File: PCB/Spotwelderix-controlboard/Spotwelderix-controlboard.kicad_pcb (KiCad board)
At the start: 2 copper layers, 103.4 x 56.4 mm, 27 parts, among them J1 Extender, J3 Switch_OnOFF, J4 FAN, P1 Display, P2 CONN_01X08, Q1 DMG1012T-7, Q2 DMG1012T-7, U1 NodeMCU32, U2 ADS1115_Module, U3 LM7805M_TO263

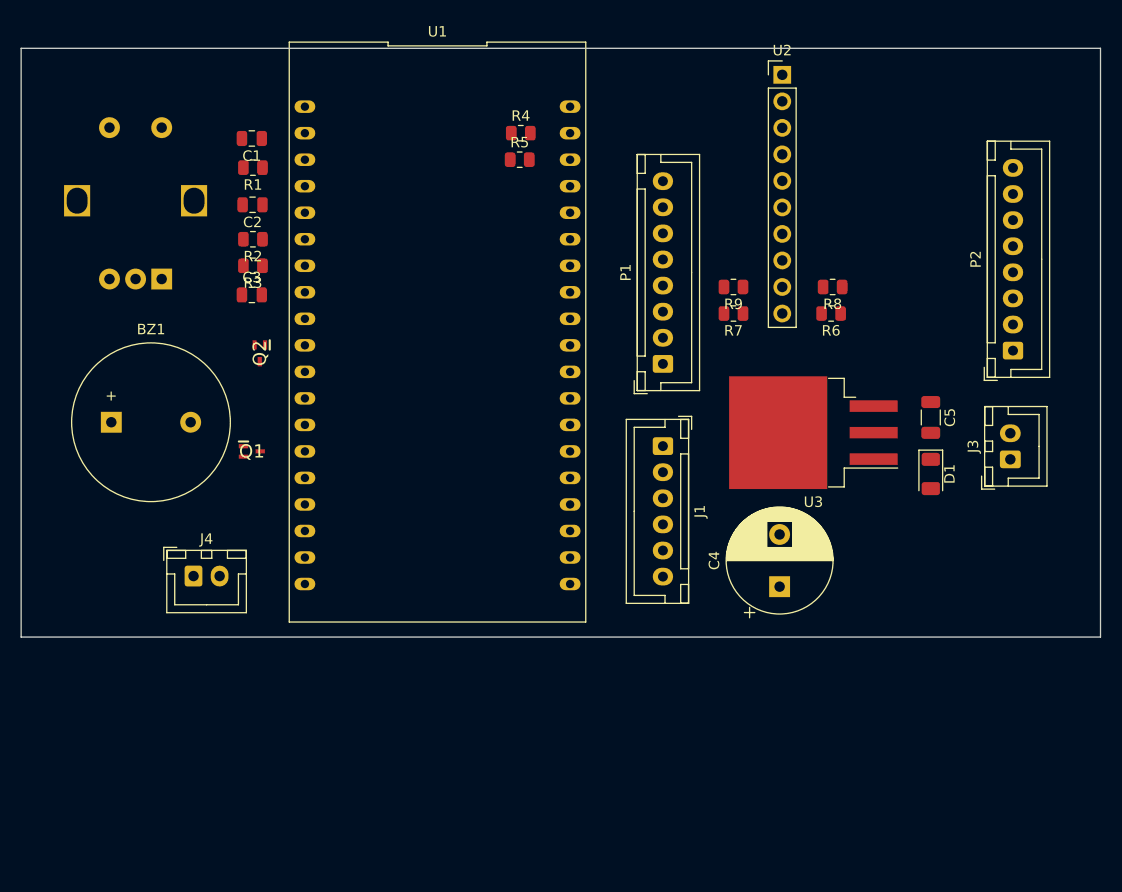
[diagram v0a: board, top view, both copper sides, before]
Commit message: power pcb added
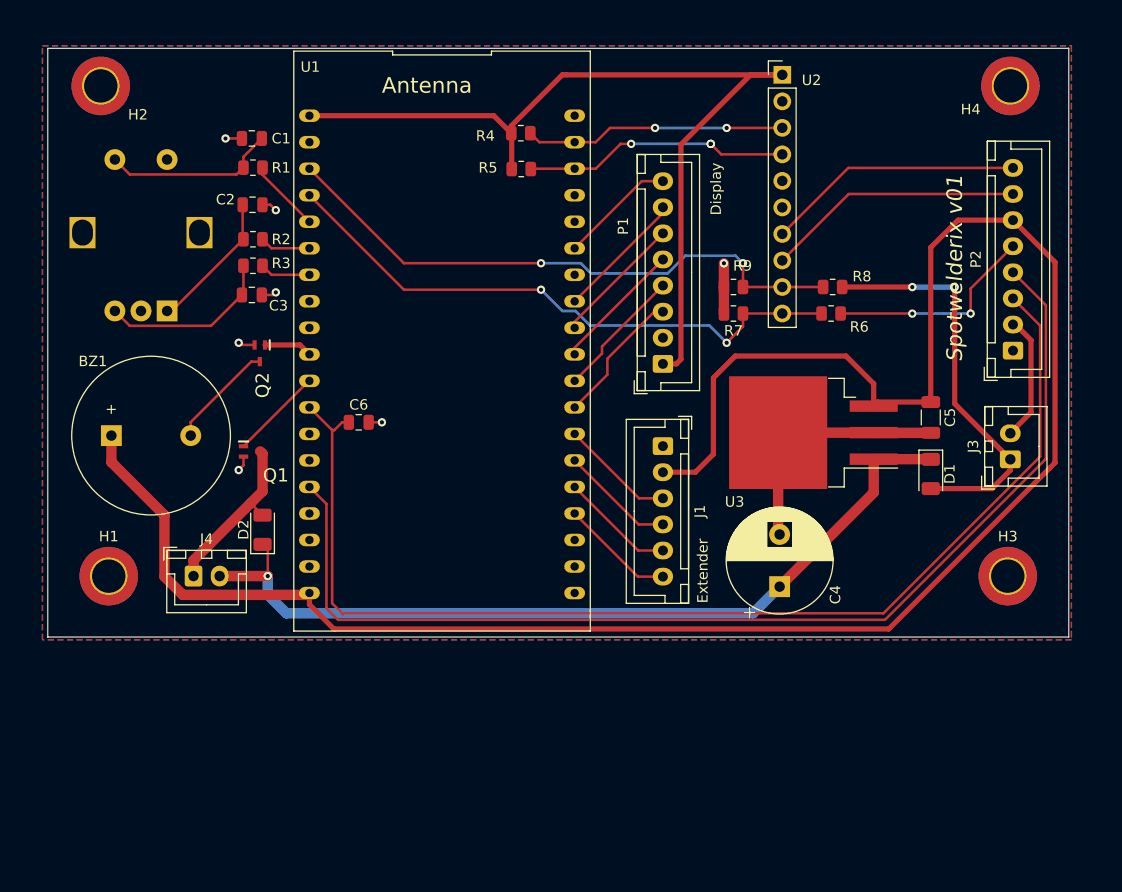
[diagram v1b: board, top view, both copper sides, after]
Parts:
- added C6: 10n, Capacitor_SMD:C_0805_2012Metric, F.Cu at (44.8, 48.3)
- added D2: D, Diode_SMD:D_1206_3216Metric, F.Cu at (35.6, 58.5)
- added H1: MountingHole, MountingHole:MountingHole_3.2mm_M3_DIN965_Pad_TopBottom, F.Cu at (20.8, 63.0)
- added H2: MountingHole, MountingHole:MountingHole_3.2mm_M3_DIN965_Pad_TopBottom, F.Cu at (20.1, 16.0)
- added H3: MountingHole, MountingHole:MountingHole_3.2mm_M3_DIN965_Pad_TopBottom, F.Cu at (106.9, 63.0)
- added H4: MountingHole, MountingHole:MountingHole_3.2mm_M3_DIN965_Pad_TopBottom, F.Cu at (107.2, 16.0)
- moved ENC1 3.10 mm to (26.4, 37.6)
- moved BZ1 1.28 mm to (21.1, 49.5)
- moved U1 0.97 mm to (52.8, 41.8)
- moved R5 0.91 mm to (60.3, 24.0)
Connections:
- J4 pad 2: +5V -> Net-(C4-Pad1)
- R4 pad 2: SDA -> SCL
- R5 pad 2: SCL -> SDA
- R6 pad 2: Net-(R6-Pad2) -> A3_VCC_ADC
- R7 pad 1: Net-(R6-Pad2) -> A3_VCC_ADC
- R8 pad 2: Net-(R8-Pad2) -> A2_ProbeADC
- R9 pad 1: Net-(R8-Pad2) -> A2_ProbeADC
- U1 pad 12: Dallas -> Gate_logic
- U1 pad 15: Gate_logic -> Dallas
- U1 pad 3: Net-(U1-Pad3) -> A2_ProbeADC
- U1 pad 36: SCL -> SDA
- U1 pad 37: SDA -> SCL
- U1 pad 4: Net-(U1-Pad4) -> A3_VCC_ADC
- U2 pad 10: Net-(R6-Pad2) -> A3_VCC_ADC
- U2 pad 9: Net-(R8-Pad2) -> A2_ProbeADC
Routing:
- net +5V: track 0.00 -> 197.0 mm
- net Gate_logic: track 0.00 -> 112.3 mm
- net Dallas: track 0.00 -> 107.2 mm
- net +3V3: track 0.00 -> 87.5 mm
- net Net-(C4-Pad1): track 0.00 -> 81.9 mm, vias 0 -> 1
- net A3_VCC_ADC: track 0.00 -> 56.8 mm, vias 0 -> 2
- net A2_ProbeADC: track 0.00 -> 56.6 mm, vias 0 -> 2
- net VCC: track 0.00 -> 38.9 mm, vias 0 -> 2
- net GND: track 0.00 -> 38.1 mm, vias 0 -> 7
- net SDA: track 0.00 -> 25.5 mm, vias 0 -> 3
- net SCL: track 0.00 -> 25.1 mm, vias 0 -> 2
- net R_Schunt_H: track 0.00 -> 24.7 mm
- net R_Schunt_L: track 0.00 -> 24.7 mm
- net Probe: track 0.00 -> 20.6 mm, vias 0 -> 2
- net Net-(C3-Pad1): track 0.00 -> 16.8 mm
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- added copper zone on F.Cu, net +5V
- added copper zone on B.Cu, net GND
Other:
- board size 103.4 x 56.4 mm -> 97.8 x 56.4 mm
- net class Default: clearance 0.3 -> 0.2
- net class Power: clearance 0.5 -> 0.3
- rule trace_clearance: 0.3 -> 0.2
- board text added: "Antenna"
- board text added: "Display"
- board text added: "Extender"
- board text added: "Spotwelderix v01"

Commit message: power pcb updated, added safe power for driver
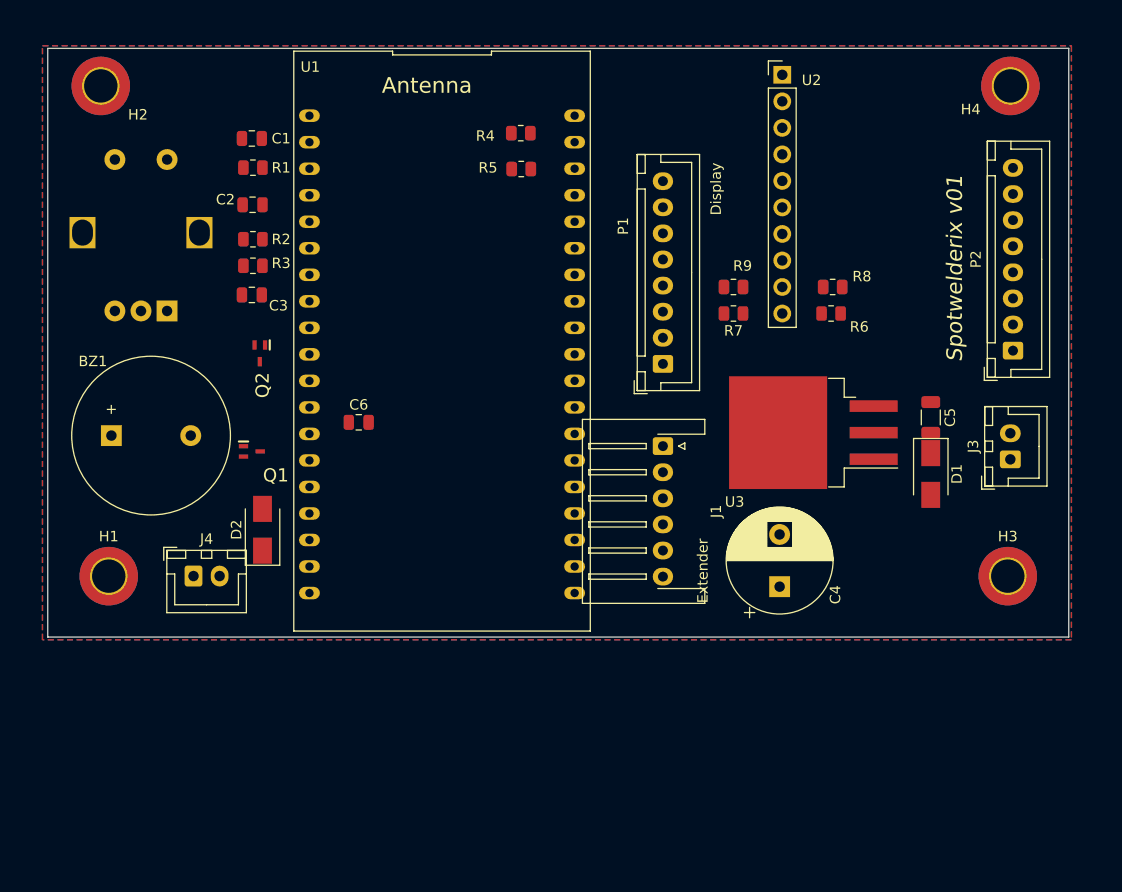
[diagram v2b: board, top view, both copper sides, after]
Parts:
- D1, D2: footprint Diode_SMD:D_1206_3216Metric -> Diode_SMD:D_SMA
- J1: footprint Connector_JST:JST_XH_B6B-XH-A_1x06_P2.50mm_Vertical -> Connector_JST:JST_XH_S6B-XH-A-1_1x06_P2.50mm_Horizontal
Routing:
- net +5V: track 197.0 -> 0.00 mm
- net Gate_logic: track 112.3 -> 0.00 mm
- net Dallas: track 107.2 -> 0.00 mm
- net +3V3: track 87.5 -> 0.00 mm
- net Net-(C4-Pad1): track 81.9 -> 0.00 mm, vias 1 -> 0
- net A3_VCC_ADC: track 56.8 -> 0.00 mm, vias 2 -> 0
- net A2_ProbeADC: track 56.6 -> 0.00 mm, vias 2 -> 0
- net VCC: track 38.9 -> 0.00 mm, vias 2 -> 0
- net GND: track 38.1 -> 0.00 mm, vias 7 -> 0
- net SDA: track 25.5 -> 0.00 mm, vias 3 -> 0
- net SCL: track 25.1 -> 0.00 mm, vias 2 -> 0
- net R_Schunt_H: track 24.7 -> 0.00 mm
- net R_Schunt_L: track 24.7 -> 0.00 mm
- net Probe: track 20.6 -> 0.00 mm, vias 2 -> 0
- net Net-(C3-Pad1): track 16.8 -> 0.00 mm
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
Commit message: ena powerpcb added
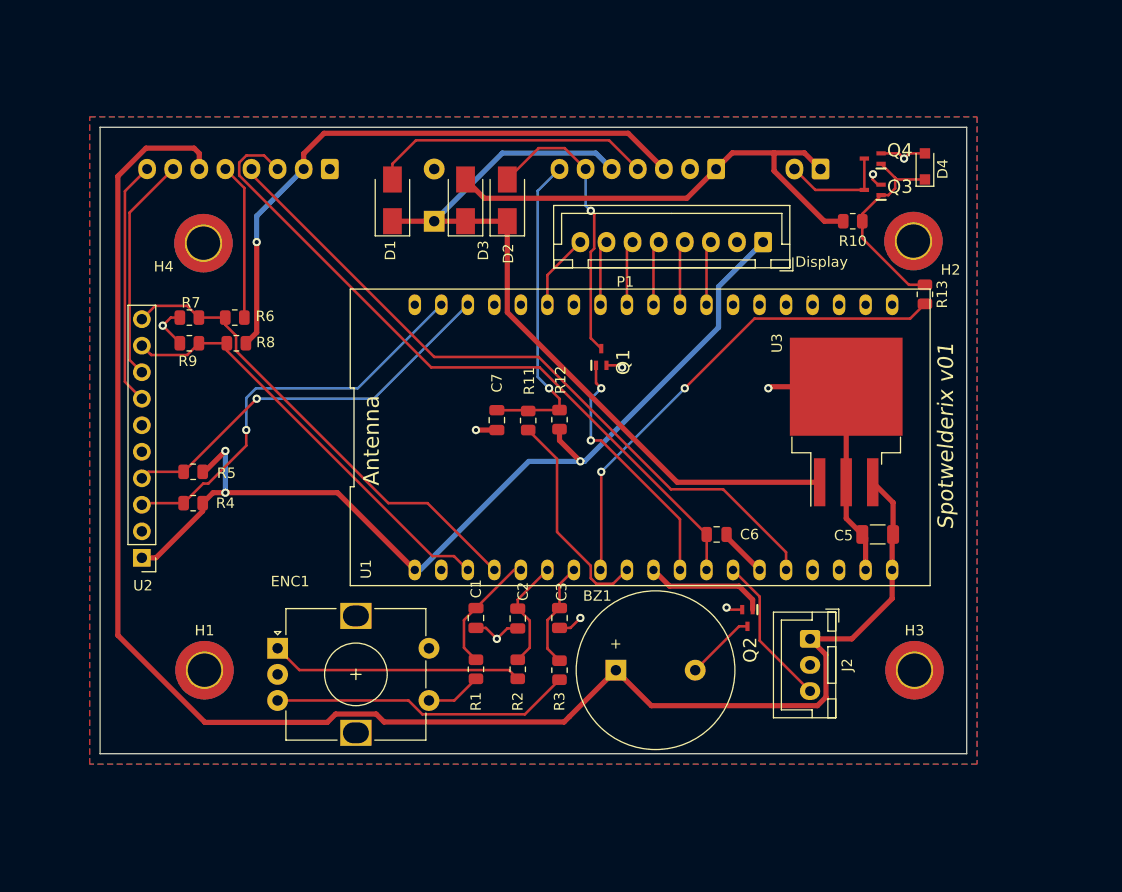
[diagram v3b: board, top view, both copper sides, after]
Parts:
- removed J1: Extender, Connector_JST:JST_XH_S6B-XH-A-1_1x06_P2.50mm_Horizontal
- added C7: 100n, Capacitor_SMD:C_0805_2012Metric, F.Cu at (58.0, 48.0)
- added D3: D, Diode_SMD:D_SMA, F.Cu at (55.0, 27.0)
- added D4: 3.6V, Diode_SMD:D_SOD-323_HandSoldering, F.Cu at (99.0, 23.8)
- added J2: LEDs, Connector_JST:JST_XH_B3B-XH-A_1x03_P2.50mm_Vertical, F.Cu at (88.0, 69.0)
- added Q3: DMG1012T-7, SamacSys_Parts:SOT50P160X80-3N, F.Cu at (94.0, 26.0)
- added Q4: DMG1012T-7, SamacSys_Parts:SOT50P160X80-3N, F.Cu at (94.0, 23.0)
- added R10: 10k, Resistor_SMD:R_0805_2012Metric, F.Cu at (92.1, 29.0)
- added R11: 100, Resistor_SMD:R_0805_2012Metric, F.Cu at (61.0, 48.1)
- added R12: 10k, Resistor_SMD:R_0805_2012Metric, F.Cu at (64.0, 48.0)
- added R13: 100, Resistor_SMD:R_0805_2012Metric, F.Cu at (99.0, 36.0)
- C1, C2, C3: value 100n -> 100p
- C4, P2: moved to B.Cu
- ENC1: moved to F.Cu
- J3: footprint Connector_JST:JST_XH_B2B-XH-A_1x02_P2.50mm_Vertical -> Connector_JST:JST_XH_B7B-XH-A_1x07_P2.50mm_Vertical; moved to B.Cu
- J4: value FAN -> Int_Charger_supply; moved to B.Cu
- moved H2 79.2 mm to (97.9, 30.9)
- moved H4 78.7 mm to (29.9, 31.1)
- moved U2 76.8 mm to (24.0, 61.2), turned to 180 degrees
- moved J4 71.6 mm to (89.0, 24.0), turned to 180 degrees
- moved P2 67.7 mm to (42.0, 24.0), turned to 180 degrees
- moved D1 57.8 mm to (48.0, 27.0), turned to 90 degrees
- moved R8 57.4 mm to (33.1, 40.7)
- moved R6 57.1 mm to (32.9, 38.2)
- moved BZ1 53.3 mm to (69.4, 72.0)
- moved Q2 53.1 mm to (82.0, 67.0)
- moved R1 52.6 mm to (56.0, 71.9), turned to 270 degrees
- moved R9 52.4 mm to (28.6, 40.7)
- moved R7 52.1 mm to (28.6, 38.2)
- moved C1 50.7 mm to (56.0, 67.0), turned to 270 degrees
- moved R3 48.6 mm to (64.0, 72.0), turned to 270 degrees
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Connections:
- C1 pad 1: Net-(C1-Pad1) -> UI_RotEnc_Push
- C2 pad 2: Net-(C2-Pad2) -> UI_RotEnc_A
- C3 pad 1: Net-(C3-Pad1) -> UI_RotEnc_B
- C4 pad 1: Net-(C4-Pad1) -> /LM7805_in
- D1 pad 1: Net-(C4-Pad1) -> /LM7805_in
- D1 pad 2: VCC -> Net-(D1-Pad2)
- D2 pad 1: Net-(C4-Pad1) -> /LM7805_in
- D2 pad 2: Net-(D2-Pad2) -> FAN_GND
- ENC1 pad A: Net-(C2-Pad2) -> Net-(ENC1-PadA)
- ENC1 pad B: Net-(C3-Pad1) -> Net-(ENC1-PadB)
- ENC1 pad S2: Net-(C1-Pad1) -> Net-(ENC1-PadS2)
- J3 pad 1: VCC -> ExtPower
- J3 pad 2: PowerVCC -> GND
- J4 pad 1: Net-(D2-Pad2) -> ExtPower
- J4 pad 2: Net-(C4-Pad1) -> Net-(J4-Pad2)
- P2 pad 2: PowerVCC -> VCC
- Q1 pad 3: Net-(D2-Pad2) -> FAN_GND
- R1 pad 2: Net-(C1-Pad1) -> Net-(ENC1-PadS2)
- R2 pad 2: Net-(C2-Pad2) -> Net-(ENC1-PadA)
- R3 pad 2: Net-(C3-Pad1) -> Net-(ENC1-PadB)
- U1 pad 13: Net-(U1-Pad13) -> LED
- U1 pad 8: Net-(U1-Pad8) -> ChargDisEna
- U1 pad 9: Net-(U1-Pad9) -> Ext_Trigger
- U3 pad 1: Net-(C4-Pad1) -> /LM7805_in
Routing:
- net +5V: track 0.00 -> 158.0 mm
- net +3V3: track 0.00 -> 91.8 mm, vias 0 -> 3
- net /LM7805_in: track 0.00 -> 76.7 mm
- net Dallas: track 0.00 -> 68.4 mm
- net Gate_logic: track 0.00 -> 68.1 mm
- net VCC: track 0.00 -> 57.2 mm, vias 0 -> 1
- net GND: track 0.00 -> 53.4 mm, vias 0 -> 9
- net ExtPower: track 0.00 -> 47.5 mm
- net ChargDisEna: track 0.00 -> 47.1 mm, vias 0 -> 2
- net A3_VCC_ADC: track 0.00 -> 46.0 mm
- net A2_ProbeADC: track 0.00 -> 41.5 mm
- net SCL: track 0.00 -> 39.3 mm, vias 0 -> 1
- net SDA: track 0.00 -> 38.1 mm, vias 0 -> 1
- net Net-(C7-Pad1): track 0.00 -> 30.9 mm, vias 0 -> 1
- net Net-(ENC1-PadB): track 0.00 -> 28.9 mm
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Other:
- board size 97.8 x 56.4 mm -> 83 x 60 mm
- board text removed: "Extender"

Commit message: ordered version v01
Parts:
- removed D1: D, Diode_SMD:D_SMA
- removed D4: 3.6V, Diode_SMD:D_SOD-323_HandSoldering
- removed J4: Int_Charger_supply, Connector_JST:JST_XH_B2B-XH-A_1x02_P2.50mm_Vertical
- removed Q3, Q4: DMG1012T-7, SamacSys_Parts:SOT50P160X80-3N
- removed R10: 10k, Resistor_SMD:R_0805_2012Metric
- removed R13: 100, Resistor_SMD:R_0805_2012Metric
- removed R4, R5: 3k3, Resistor_SMD:R_0805_2012Metric
- removed U2: ADS1115_Module, Connector_PinHeader_2.54mm:PinHeader_1x10_P2.54mm_Vertical
- added J1: ChargerPower, Connector_JST:JST_XH_S5B-XH-A_1x05_P2.50mm_Horizontal, F.Cu at (34.8, 68.3)
- added Q5: AO3400A, Package_TO_SOT_SMD:SOT-23, F.Cu at (55.1, 31.9)
- added R14: 100, Resistor_SMD:R_0805_2012Metric, F.Cu at (29.9, 66.5)
- C7: value 100n -> 100p
- J3: value Switch_OnOFF -> ExtPwr_FAn; footprint Connector_JST:JST_XH_B7B-XH-A_1x07_P2.50mm_Vertical -> Connector_JST:JST_XH_B4B-XH-A_1x04_P2.50mm_Vertical
- P1: footprint Connector_JST:JST_XH_B8B-XH-A_1x08_P2.50mm_Vertical -> Connector_JST:JST_XH_S8B-XH-A_1x08_P2.50mm_Horizontal
- P2: value CONN_01X08 -> PowerPCB; footprint Connector_JST:JST_XH_B8B-XH-A_1x08_P2.50mm_Vertical -> Connector_JST:JST_XH_B9B-XH-A_1x09_P2.50mm_Vertical
- Q1, Q2: value DMG1012T-7 -> AO3400A; footprint SamacSys_Parts:SOT50P160X80-3N -> Package_TO_SOT_SMD:SOT-23
- R11: value 100 -> 33k
- moved P1 55.1 mm to (29.6, 42.2), turned to 270 degrees
- moved BZ1 47.4 mm to (37.0, 37.4)
- moved J3 47.3 mm to (31.8, 24.5)
- moved R9 41.9 mm to (70.2, 36.3), turned to 270 degrees
- moved R7 38.9 mm to (67.4, 36.2), turned to 270 degrees
- moved R8 38.2 mm to (70.2, 31.8), turned to 270 degrees
- moved U3 36.4 mm to (63.0, 71.0), turned to 270 degrees
- moved R6 35.1 mm to (67.4, 31.9), turned to 270 degrees
- moved P2 34.4 mm to (76.4, 24.4)
- moved C5 32.9 mm to (61.6, 61.0), turned to 0 degrees
- moved C7 32.4 mm to (29.9, 64.2), turned to 0 degrees
- moved Q2 30.2 mm to (61.0, 45.4), turned to 180 degrees
- moved J2 28.7 mm to (81.8, 41.0)
- moved Q1 24.3 mm to (54.8, 62.5), turned to 180 degrees
- moved R11 22.1 mm to (46.1, 64.5), turned to 0 degrees
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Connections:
- C4 pad 1: /LM7805_in -> VCC
- C7 pad 1: Net-(C7-Pad1) -> FootSwitch
- D2 pad 1: /LM7805_in -> VCC
- D3 pad 1: /LM7805_in -> VCC
- J3 pad 4: Net-(D1-Pad2) -> FAN_GND
- P2 pad 6: +5V -> Vbat_ADC
- P2 pad 7: R_Schunt_H -> EnableSupply
- P2 pad 8: R_Schunt_L -> +5V
- Q1 pad 1: FAN -> ChargerEna
- Q1 pad 3: FAN_GND -> Net-(J1-Pad4)
- R11 pad 1: Net-(C7-Pad1) -> ExtPower
- R11 pad 2: Ext_Trigger -> ExtPWRADC
- R12 pad 1: +3V3 -> ExtPWRADC
- R12 pad 2: Net-(C7-Pad1) -> GND
- R6 pad 2: A3_VCC_ADC -> ProbeADC
- R7 pad 1: A3_VCC_ADC -> ProbeADC
- R8 pad 2: A2_ProbeADC -> VCC_ADC
- R9 pad 1: A2_ProbeADC -> VCC_ADC
- U1 pad 24: Net-(U1-Pad24) -> ChargerEna
- U1 pad 26: Net-(U1-Pad26) -> FootSwitch
- U1 pad 3: A2_ProbeADC -> UI_RotEnc_B
- U1 pad 36: SDA -> EnableSupply
- U1 pad 37: SCL -> UI_RotEnc_Push
- U1 pad 4: A3_VCC_ADC -> UI_RotEnc_A
- U1 pad 5: UI_RotEnc_Push -> Vbat_ADC
- U1 pad 6: UI_RotEnc_A -> ProbeADC
- U1 pad 7: UI_RotEnc_B -> VCC_ADC
- U1 pad 8: ChargDisEna -> Shuntvoltage
- U1 pad 9: Ext_Trigger -> ExtPWRADC
- U3 pad 1: /LM7805_in -> VCC
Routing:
- net VCC: track 57.2 -> 167.8 mm, vias 1 -> 0
- net /LM7805_in: track 76.7 -> 0.00 mm
- net EnableSupply: track 0.00 -> 51.3 mm, vias 0 -> 2
- net Dallas: track 68.4 -> 20.1 mm, vias 0 -> 1
- net ChargDisEna: track 47.1 -> 0.00 mm, vias 2 -> 0
- net Vbat_ADC: track 0.00 -> 46.7 mm, vias 0 -> 1
- net A3_VCC_ADC: track 46.0 -> 0.00 mm
- net ExtPWRADC: track 0.00 -> 44.7 mm, vias 0 -> 2
- net Shuntvoltage: track 0.00 -> 42.4 mm, vias 0 -> 2
- net A2_ProbeADC: track 41.5 -> 0.00 mm
- net SCL: track 39.3 -> 0.00 mm, vias 1 -> 0
- net Gate_logic: track 68.1 -> 29.5 mm
- net SDA: track 38.1 -> 0.00 mm, vias 1 -> 0
- net FootSwitch: track 0.00 -> 37.4 mm
- net ProbeADC: track 0.00 -> 34.5 mm, vias 0 -> 1
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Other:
- board size 83 x 60 mm -> 65.6 x 60 mm
- board text added: "ExtPwr-FtSwt"
- board text added: "LED"
